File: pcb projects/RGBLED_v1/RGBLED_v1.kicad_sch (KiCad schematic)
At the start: 20 parts, among them J1 USB_B_Micro, J2 Conn_01x02_Pin, SW1 SW_Reed_SPDT, SW2 RESET BUTTON, U1 STM32F091RBTx, U2 LP3985IM5-3.3/NOPB

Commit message: changed switch, added swd jpg
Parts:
- removed SW1: SW_Reed_SPDT, symbol Switch:SW_Reed_SPDT
- added SW1: SW_DP3T, symbol Switch:SW_DP3T
- SW2: symbol Switch:SW_Push_Open_Dual -> Switch:SW_Push_Dual
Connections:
- net +3.3V: now also SW1.3
- net GND: now also SW2.1; no longer SW2.4
- net at C2.1, U2.5 (OUT): now also SW1.1
- net at BT1.1 (+): now also SW1.2
- no-connect marks 3 -> 4
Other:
- moved on the sheet: BT1

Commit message: board drawing, footprints except slide switch
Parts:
- added C9: 22nF, Capacitor_SMD:C_0805_2012Metric_Pad1.18x1.45mm_HandSolder, symbol Device:C
- BT1: footprint (none) -> Battery:BatteryHolder_MYOUNG_BS-07-A1BJ001_CR2032
- CN2: renamed from J2; value Conn_01x02_Pin -> Conn_01x03_Pin; footprint (none) -> Connector_PinHeader_2.54mm:PinHeader_1x03_P2.54mm_Vertical; symbol Connector:Conn_01x02_Pin -> Connector_Generic:Conn_01x03
- SW2: footprint (none) -> Button_Switch_SMD:SW_Push_1P1T_NO_E-Switch_TL3301NxxxxxG
- renumbered J1 to CN1
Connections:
- net GND: now also CN2.3 (Pin_3), C9.2
- net TCK: now also CN2.1 (Pin_1); no longer CN2.2 (Pin_2)
- net TMS: now also CN2.2 (Pin_2); no longer CN2.1 (Pin_1)
- net at BT1.1 (+), SW1.2: now also C9.1
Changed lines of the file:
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@@
+	)
+	(junction
+		(at 77.47 64.77)
+		(diameter 0)
+		(color 0 0 0 0)
 	)
 	(junction
@@
 	)
 	(junction
+		(at 77.47 76.2)
+		(diameter 0)
+		(color 0 0 0 0)
+	)
+	(junction
 		(at 220.98 151.13)
 		(diameter 0)
@@
 	(wire
 		(pts
+			(xy 77.47 64.77) (xy 77.47 68.58)
+		)
+		(stroke
+			(width 0)
+			(type default)
+		)
+	)
+	(wire
+		(pts
 			(xy 55.88 33.02) (xy 58.42 33.02)
 		)
@@
 	(wire
 		(pts
+			(xy 36.83 138.43) (xy 31.75 138.43)
+		)
+		(stroke
+			(width 0)
+			(type default)
+		)
+	)
+	(wire
+		(pts
 			(xy 229.87 33.02) (xy 243.84 33.02)
 		)
@@
 	(wire
 		(pts
+			(xy 31.75 138.43) (xy 31.75 139.7)
+		)
+		(stroke
+			(width 0)
+			(type default)
+		)
+	)
+	(wire
+		(pts
 			(xy 220.98 151.13) (xy 223.52 151.13)
 		)
@@
 	(wire
 		(pts
+			(xy 77.47 76.2) (xy 85.09 76.2)
+		)
+		(stroke
+			(width 0)
+			(type default)
+		)
+	)
+	(wire
+		(pts
 			(xy 215.9 54.61) (xy 215.9 50.8)
 		)
@@
 	(wire
 		(pts
-			(xy 77.47 57.15) (xy 77.47 68.58)
+			(xy 77.47 57.15) (xy 77.47 64.77)
 		)
 		(stroke
@@
 		(pts
 			(xy 24.13 54.61) (xy 31.75 54.61)
+		)
+		(stroke
+			(width 0)
+			(type default)
+		)
+	)
+	(wire
+		(pts
+			(xy 85.09 64.77) (xy 77.47 64.77)
+		)
+		(stroke
+			(width 0)
+			(type default)
+		)
+	)
+	(wire
+		(pts
+			(xy 85.09 68.58) (xy 85.09 64.77)
 		)
 		(stroke
@@
 			)
 		)
-		(property "Footprint" ""
+		(property "Footprint" "Button_Switch_SMD:SW_Push_1P1T_NO_E-Switch_TL3301NxxxxxG"
 			(at 39.37 100.33 0)
 			(effects
@@
 	)
 	(symbol
+		(lib_id "Device:C")
+		(at 85.09 72.39 0)
+		(unit 1)
+		(exclude_from_sim no)
+		(in_bom yes)
+		(on_board yes)
+		(dnp no)
+		(fields_autoplaced yes)
+		(property "Reference" "C9"
+			(at 88.9 71.1199 0)
+			(effects
+				(font
+					(size 1.27 1.27)
+				)
+				(justify left)
+			)
+		)
+		(property "Value" "22nF"
+			(at 88.9 73.6599 0)
+			(effects
+				(font
+					(size 1.27 1.27)
+				)
+				(justify left)
+			)
+		)
+		(property "Footprint" "Capacitor_SMD:C_0805_2012Metric_Pad1.18x1.45mm_HandSolder"
+			(at 86.0552 76.2 0)
+			(effects
+				(font
+					(size 1.27 1.27)
+				)
+				(hide yes)
+			)
+		)
+		(property "Datasheet" "~"
+			(at 85.09 72.39 0)
+			(effects
+				(font
+					(size 1.27 1.27)
+				)
+				(hide yes)
+			)
+		)
+		(property "Description" "Unpolarized capacitor"
+			(at 85.09 72.39 0)
+			(effects
+				(font
+					(size 1.27 1.27)
+				)
+				(hide yes)
+			)
+		)
+		(pin "2"
+		)
+		(pin "1"
+		)
+		(instances
+			(project ""
+				(path "/776e18e0-dd51-4c38-87d7-7b7a4ed2b66e"
+					(reference "C9")
+					(unit 1)
+				)
+			)
+		)
+	)
+	(symbol
 		(lib_id "power:+3.3V")
 		(at 229.87 21.59 0)
@@
 	)
 	(symbol
-		(lib_id "power:+3.3V")
-		(at 198.12 54.61 0)
-		(unit 1)
-		(exclude_from_sim no)
-		(in_bom yes)
-		(on_board yes)
-		(dnp no)
-		(fields_autoplaced yes)
-		(property "Reference" "#PWR012"
-			(at 198.12 58.42 0)
-			(effects
-				(font
-					(size 1.27 1.27)
-				)
-				(hide yes)
-			)
-		)
-		(property "Value" "+3.3V"
-			(at 198.12 49.53 0)
-			(effects
-				(font
-					(size 1.27 1.27)
-				)
-			)
-		)
-		(property "Footprint" ""
-			(at 198.12 54.61 0)
-			(effects
-				(font
-					(size 1.27 1.27)
-				)
-				(hide yes)
-			)
-		)
-		(property "Datasheet" ""
-			(at 198.12 54.61 0)
-			(effects
-				(font
-					(size 1.27 1.27)
-				)
-				(hide yes)
-			)
-		)
-		(property "Description" "Power symbol creates a global label with name \"+3.3V\""
-			(at 198.12 54.61 0)
-			(effects
-				(font
-					(size 1.27 1.27)
-				)
-				(hide yes)
-			)
-		)
-		(pin "1"
-		)
-		(instances
-			(project "RGBLED_v1"
-				(path "/776e18e0-dd51-4c38-87d7-7b7a4ed2b66e"
-					(reference "#PWR012")
-					(unit 1)
-				)
-			)
-		)
-	)
-	(symbol
 		(lib_id "Device:Battery_Cell")
 		(at 77.47 73.66 0)
@@
 			)
 		)
-		(property "Footprint" ""
+		(property "Footprint" "Battery:BatteryHolder_MYOUNG_BS-07-A1BJ001_CR2032"
 			(at 77.47 72.136 90)
 			(effects
@@
 		(dnp no)
 		(fields_autoplaced yes)
-		(property "Reference" "J1"
-			(at 36.83 29.2099 90)
+		(property "Reference" "CN1"
+			(at 36.83 30.4799 90)
 			(effects
 				(font
@@
 				)
 				(justify left)
+				(hide yes)
 			)
 		)
@@
 			(project ""
 				(path "/776e18e0-dd51-4c38-87d7-7b7a4ed2b66e"
-					(reference "J1")
+					(reference "CN1")
 					(unit 1)
 				)
@@
 	)
 	(symbol
-		(lib_id "Connector:Conn_01x02_Pin")
-		(at 41.91 135.89 180)
+		(lib_id "Connector_Generic:Conn_01x03")
+		(at 41.91 135.89 0)
 		(unit 1)
 		(exclude_from_sim no)
@@
 		(dnp no)
 		(fields_autoplaced yes)
-		(property "Reference" "J2"
-			(at 43.18 133.3499 0)
-			(effects
-				(font
-					(size 1.27 1.27)
-				)
-				(justify right)
-			)
-		)
-		(property "Value" "Conn_01x02_Pin"
-			(at 43.18 135.8899 0)
-			(effects
-				(font
-					(size 1.27 1.27)
-				)
-				(justify right)
-			)
-		)
-		(property "Footprint" ""
+		(property "Reference" "CN2"
+			(at 44.45 135.8899 0)
+			(effects
+				(font
+					(size 1.27 1.27)
+				)
+				(justify left)
+			)
+		)
+		(property "Value" "Conn_01x03_Pin"
+			(at 44.45 137.1599 0)
+			(effects
+				(font
+					(size 1.27 1.27)
+				)
+				(justify left)
+				(hide yes)
+			)
+		)
+		(property "Footprint" "Connector_PinHeader_2.54mm:PinHeader_1x03_P2.54mm_Vertical"
 			(at 41.91 135.89 0)
 			(effects
@@
 			)
 		)
-		(property "Description" "Generic connector, single row, 01x02, script generated"
+		(property "Description" "Generic connector, single row, 01x03, script generated (kicad-library-utils/schlib/autogen/connector/)"
 			(at 41.91 135.89 0)
 			(effects
@@
 		)
 		(pin "2"
+		)
+		(pin "3"
 		)
 		(instances
 			(project ""
 				(path "/776e18e0-dd51-4c38-87d7-7b7a4ed2b66e"
-					(reference "J2")
+					(reference "CN2")
 					(unit 1)
 				)
@@
 					(unit 1)
 				)
+			)
+		)
+	)
+	(symbol
+		(lib_id "power:GND")
+		(at 31.75 139.7 0)
+		(mirror y)
+		(unit 1)
+		(exclude_from_sim no)
+		(in_bom yes)
+		(on_board yes)
+		(dnp no)
+		(fields_autoplaced yes)
+		(property "Reference" "#PWR015"
+			(at 31.75 146.05 0)
+			(effects
+				(font
+					(size 1.27 1.27)
+				)
+				(hide yes)
+			)
+		)
+		(property "Value" "GND"
+			(at 31.75 144.78 0)
+			(effects
+				(font
+					(size 1.27 1.27)
+				)
+			)
+		)
+		(property "Footprint" ""
+			(at 31.75 139.7 0)
+			(effects
+				(font
+					(size 1.27 1.27)
+				)
+				(hide yes)
+			)
+		)
+		(property "Datasheet" ""
+			(at 31.75 139.7 0)
+			(effects
+				(font
+					(size 1.27 1.27)
+				)
+				(hide yes)
+			)
+		)
+		(property "Description" "Power symbol creates a global label with name \"GND\" , ground"
+			(at 31.75 139.7 0)
+			(effects
+				(font
+					(size 1.27 1.27)
+				)
+				(hide yes)
+			)
+		)
+		(pin "1"
+		)
+		(instances
+			(project "RGBLED_v1"
+				(path "/776e18e0-dd51-4c38-87d7-7b7a4ed2b66e"
+					(reference "#PWR015")
+					(unit 1)
+				)

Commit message: mcu finished
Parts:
- removed SW1: SW_DP3T, symbol Switch:SW_DP3T
- removed SW2: RESET BUTTON, Button_Switch_SMD:SW_Push_1P1T_NO_E-Switch_TL3301NxxxxxG, symbol Switch:SW_Push_Dual
- added C10, C11: 4.3pF, Capacitor_SMD:C_1206_3216Metric_Pad1.33x1.80mm_HandSolder, symbol Device:C
- added C12: 100nF, symbol Device:C
- added J1: Conn_02x02_Odd_Even, Connector_PinHeader_2.54mm:PinHeader_2x02_P2.54mm_Vertical, symbol Connector_Generic:Conn_02x02_Odd_Even
- added JP1: SolderJumper, Jumper:SolderJumper-2_P1.3mm_Open_TrianglePad1.0x1.5mm, symbol Jumper:SolderJumper_2_Open
- added L1: Ferrite, symbol Device:L
- added SW1: SW_MEC_5E, Button_Switch_SMD:SW_MEC_5GSH9, symbol Switch:SW_MEC_5E
- added Y1: 32.768kHz, Crystal:Crystal_SMD_HC49-SD_HandSoldering, symbol Device:Crystal
- C4, C5, C6, C7, C8: value 0.01uF -> 100nF
- C9: footprint Capacitor_SMD:C_0805_2012Metric_Pad1.18x1.45mm_HandSolder -> Capacitor_SMD:C_1206_3216Metric_Pad1.33x1.80mm_HandSolder
- CN2: footprint Connector_PinHeader_2.54mm:PinHeader_1x03_P2.54mm_Vertical -> Connector_PinHeader_2.54mm:PinHeader_1x04_P2.54mm_Vertical; symbol Connector_Generic:Conn_01x03 -> Connector_Generic:Conn_01x04
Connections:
- net +3.3V: now also CN2.1 (Pin_1), J1.2 (Pin_2), J1.4 (Pin_4), L1.1; no longer C7.2, U1.13 (VDDA), U1.48 (VDDIO2)
- net GND: now also CN2.4 (Pin_4), C10.1, C11.2, C12.1, JP1.1 (A), SW1.1, SW1.2; no longer C7.1, CN2.3 (Pin_3), U1.12 (VSSA)
- net TCK: now also CN2.2 (Pin_2); no longer CN2.1 (Pin_1)
- net TMS: now also CN2.3 (Pin_3); no longer CN2.2 (Pin_2)
- net nRST: now also C12.2, SW1.3 (K), SW1.4 (A)
- net at U1.3 (PC14): now also C10.2, Y1.2
- net at U1.4 (PC15): now also C11.1, Y1.1
- net at C2.1, U2.5 (OUT): now also J1.1 (Pin_1)
- net at BT1.1 (+), C9.1: now also J1.3 (Pin_3)
- new net AVDD: C7.2, L1.2, U1.13 (VDDA)
- new net GNDA: C7.1, JP1.2 (B), U1.12 (VSSA)
- no-connect marks 4 -> 3
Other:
- moved on the sheet: C7

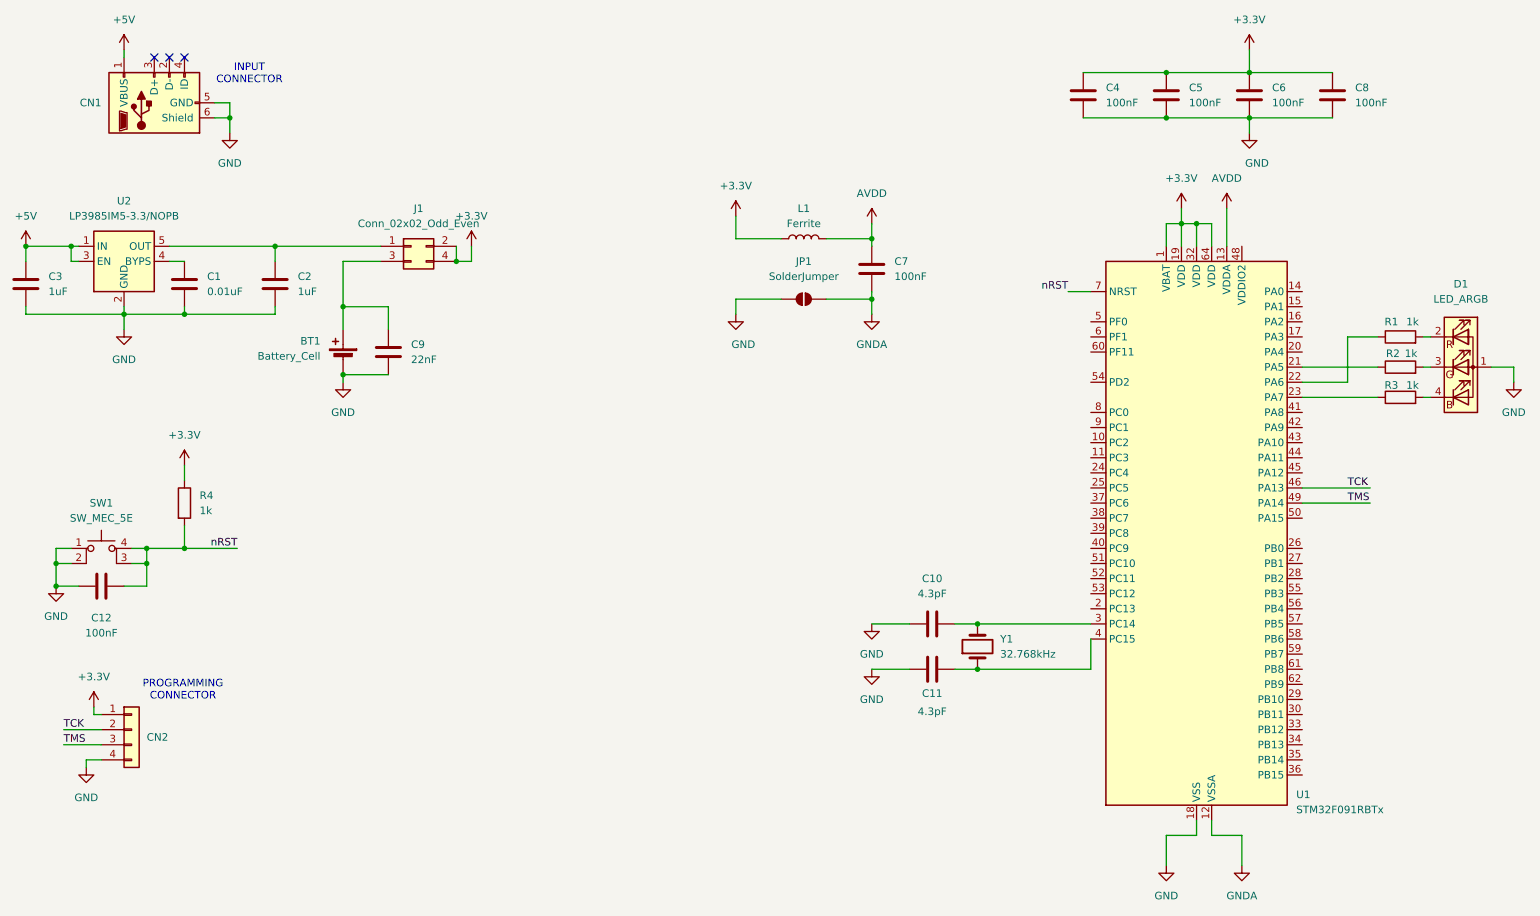
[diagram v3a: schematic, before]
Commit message: components placement
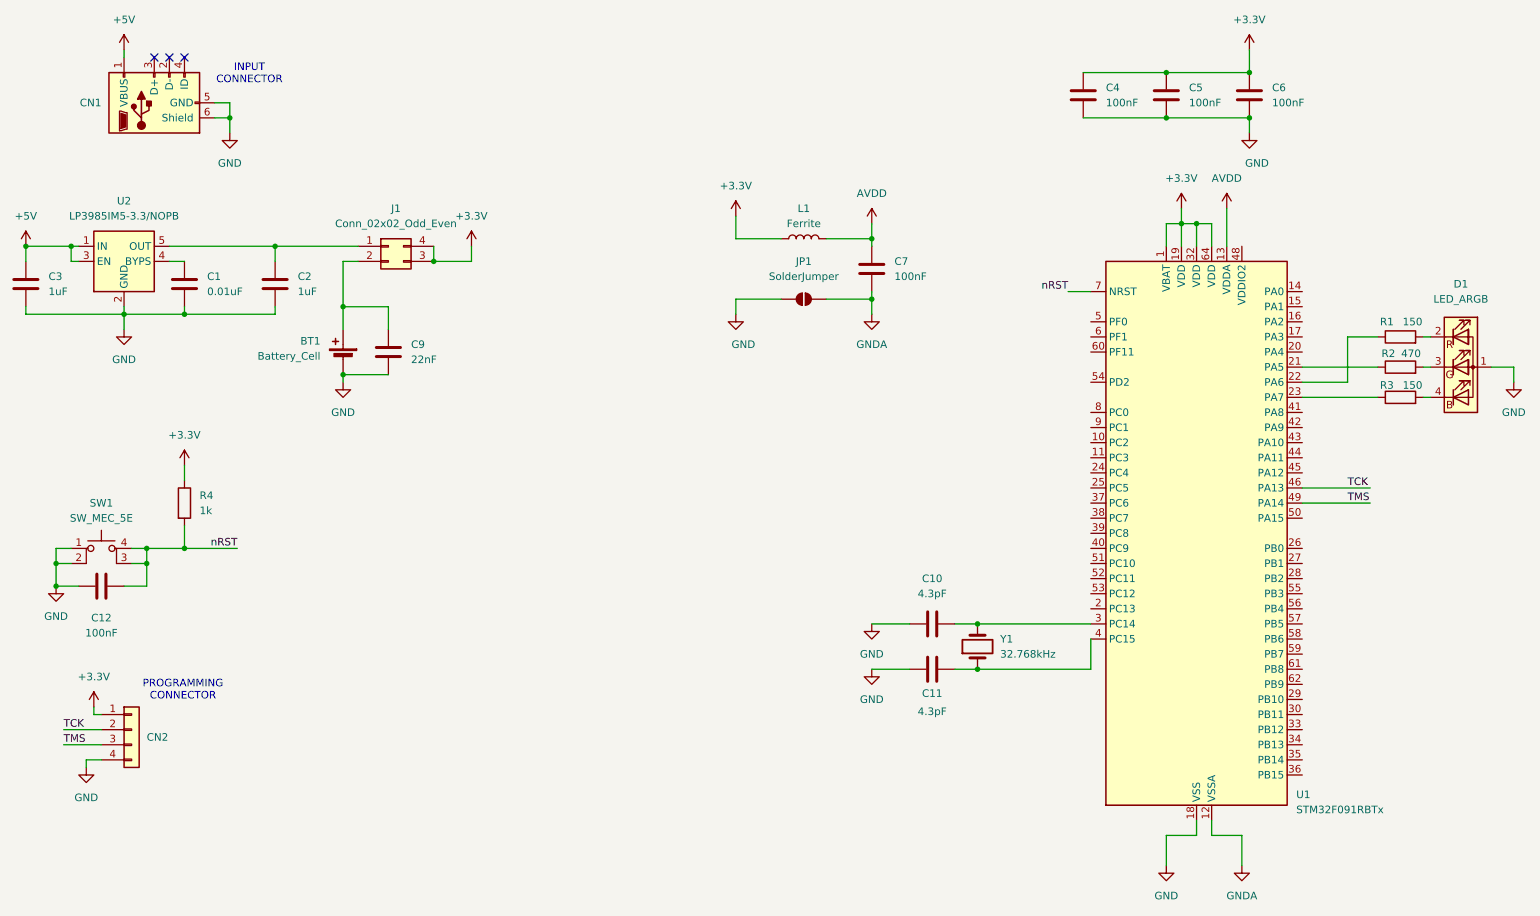
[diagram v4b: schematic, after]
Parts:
- removed C8: 100nF, Capacitor_SMD:C_1206_3216Metric_Pad1.33x1.80mm_HandSolder, symbol Device:C
- J1: symbol Connector_Generic:Conn_02x02_Odd_Even -> Connector_Generic:Conn_02x02_Counter_Clockwise
- R1, R3: value 1k -> 150
- R2: value 1k -> 470
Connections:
- net +3.3V: now also J1.3 (Pin_3); no longer J1.2 (Pin_2)
- net at BT1.1 (+), C9.1: now also J1.2 (Pin_2); no longer J1.3 (Pin_3)
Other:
- moved on the sheet: J1
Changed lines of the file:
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@@
 	)
 	(junction
-		(at 66.04 54.61)
+		(at 220.98 50.8)
 		(diameter 0)
 		(color 0 0 0 0)
 	)
 	(junction
-		(at 220.98 50.8)
+		(at 184.15 125.73)
 		(diameter 0)
 		(color 0 0 0 0)
 	)
 	(junction
-		(at 184.15 125.73)
+		(at 66.04 54.61)
 		(diameter 0)
 		(color 0 0 0 0)
@@
 	)
 	(junction
-		(at 96.52 57.15)
-		(diameter 0)
-		(color 0 0 0 0)
-	)
-	(junction
 		(at 40.64 66.04)
 		(diameter 0)
@@
 	)
 	(junction
+		(at 92.71 57.15)
+		(diameter 0)
+		(color 0 0 0 0)
+	)
+	(junction
 		(at 229.87 33.02)
 		(diameter 0)
@@
 	(wire
 		(pts
-			(xy 223.52 50.8) (xy 223.52 54.61)
+			(xy 92.71 54.61) (xy 92.71 57.15)
 		)
 		(stroke
@@
 	(wire
 		(pts
-			(xy 24.13 64.77) (xy 24.13 66.04)
+			(xy 223.52 50.8) (xy 223.52 54.61)
 		)
 		(stroke
@@
 	(wire
 		(pts
-			(xy 66.04 66.04) (xy 50.8 66.04)
+			(xy 24.13 64.77) (xy 24.13 66.04)
 		)
 		(stroke
@@
 	(wire
 		(pts
-			(xy 203.2 120.65) (xy 203.2 125.73)
+			(xy 66.04 66.04) (xy 50.8 66.04)
 		)
 		(stroke
@@
 	(wire
 		(pts
-			(xy 34.29 140.97) (xy 36.83 140.97)
+			(xy 203.2 120.65) (xy 203.2 125.73)
 		)
 		(stroke
@@
 	(wire
 		(pts
-			(xy 29.21 107.95) (xy 29.21 111.76)
+			(xy 34.29 140.97) (xy 36.83 140.97)
 		)
 		(stroke
@@
 	(wire
 		(pts
-			(xy 238.76 80.01) (xy 251.46 80.01)
+			(xy 29.21 107.95) (xy 29.21 111.76)
 		)
 		(stroke
@@
 	(wire
 		(pts
-			(xy 228.6 153.67) (xy 223.52 153.67)
+			(xy 238.76 80.01) (xy 251.46 80.01)
 		)
 		(stroke
@@
 	(wire
 		(pts
-			(xy 229.87 33.02) (xy 243.84 33.02)
+			(xy 228.6 153.67) (xy 223.52 153.67)
 		)
 		(stroke
@@
 	(wire
 		(pts
-			(xy 77.47 57.15) (xy 83.82 57.15)
+			(xy 77.47 57.15) (xy 80.01 57.15)
 		)
 		(stroke
@@
 	(wire
 		(pts
-			(xy 66.04 54.61) (xy 83.82 54.61)
-		)
-		(stroke
-			(width 0)
-			(type default)
-		)
-	)
-	(wire
-		(pts
 			(xy 29.21 105.41) (xy 29.21 107.95)
 		)
@@
 	(wire
 		(pts
-			(xy 229.87 25.4) (xy 243.84 25.4)
-		)
-		(stroke
-			(width 0)
-			(type default)
-		)
-	)
-	(wire
-		(pts
 			(xy 77.47 76.2) (xy 85.09 76.2)
 		)
@@
 	(wire
 		(pts
-			(xy 96.52 57.15) (xy 99.06 57.15)
+			(xy 24.13 54.61) (xy 31.75 54.61)
 		)
 		(stroke
@@
 	(wire
 		(pts
-			(xy 24.13 54.61) (xy 31.75 54.61)
+			(xy 85.09 64.77) (xy 77.47 64.77)
 		)
 		(stroke
@@
 	(wire
 		(pts
-			(xy 85.09 64.77) (xy 77.47 64.77)
+			(xy 143.51 63.5) (xy 143.51 66.04)
 		)
 		(stroke
@@
 	(wire
 		(pts
-			(xy 143.51 63.5) (xy 143.51 66.04)
+			(xy 85.09 68.58) (xy 85.09 64.77)
 		)
 		(stroke
@@
 	(wire
 		(pts
-			(xy 96.52 54.61) (xy 96.52 57.15)
+			(xy 66.04 54.61) (xy 80.01 54.61)
 		)
 		(stroke
@@
 	(wire
 		(pts
-			(xy 85.09 68.58) (xy 85.09 64.77)
+			(xy 31.75 54.61) (xy 33.02 54.61)
 		)
 		(stroke
@@
 	(wire
 		(pts
-			(xy 31.75 54.61) (xy 33.02 54.61)
+			(xy 92.71 57.15) (xy 99.06 57.15)
 		)
 		(stroke
@@
 		(dnp no)
 		(property "Reference" "R2"
-			(at 254 72.644 90)
+			(at 253.238 72.644 90)
 			(effects
 				(font
@@
 			)
 		)
-		(property "Value" "1k"
+		(property "Value" "470"
 			(at 257.048 72.644 90)
 			(effects
@@
 	)
 	(symbol
-		(lib_id "Device:C")
-		(at 243.84 29.21 180)
-		(unit 1)
-		(exclude_from_sim no)
-		(in_bom yes)
-		(on_board yes)
-		(dnp no)
-		(fields_autoplaced yes)
-		(property "Reference" "C8"
-			(at 247.65 27.9399 0)
-			(effects
-				(font
-					(size 1.27 1.27)
-				)
-				(justify right)
-			)
-		)
-		(property "Value" "100nF"
-			(at 247.65 30.4799 0)
-			(effects
-				(font
-					(size 1.27 1.27)
-				)
-				(justify right)
-			)
-		)
-		(property "Footprint" "Capacitor_SMD:C_1206_3216Metric_Pad1.33x1.80mm_HandSolder"
-			(at 242.8748 25.4 0)
-			(effects
-				(font
-					(size 1.27 1.27)
-				)
-				(hide yes)
-			)
-		)
-		(property "Datasheet" "~"
-			(at 243.84 29.21 0)
-			(effects
-				(font
-					(size 1.27 1.27)
-				)
-				(hide yes)
-			)
-		)
-		(property "Description" "Unpolarized capacitor"
-			(at 243.84 29.21 0)
-			(effects
-				(font
-					(size 1.27 1.27)
-				)
-				(hide yes)
-			)
-		)
-		(pin "2"
-		)
-		(pin "1"
-		)
-		(instances
-			(project "RGBLED_v1"
-				(path "/776e18e0-dd51-4c38-87d7-7b7a4ed2b66e"
-					(reference "C8")
-					(unit 1)
-				)
-			)
-		)
-	)
-	(symbol
 		(lib_id "power:GND")
 		(at 29.21 111.76 0)
@@
 		(dnp no)
 		(property "Reference" "R3"
-			(at 253.746 77.978 90)
+			(at 252.984 77.978 90)
 			(effects
 				(font
@@
 			)
 		)
-		(property "Value" "1k"
+		(property "Value" "150"
 			(at 257.302 77.978 90)
 			(effects
@@
 	)
 	(symbol
-		(lib_id "Connector_Generic:Conn_02x02_Odd_Even")
-		(at 88.9 54.61 0)
+		(lib_id "Connector_Generic:Conn_02x02_Counter_Clockwise")
+		(at 85.09 54.61 0)
 		(unit 1)
 		(exclude_from_sim no)
@@
 		(fields_autoplaced yes)
 		(property "Reference" "J1"
-			(at 90.17 48.26 0)
+			(at 86.36 48.26 0)
 			(effects
 				(font
@@
 		)
 		(property "Value" "Conn_02x02_Odd_Even"
-			(at 90.17 50.8 0)
+			(at 86.36 50.8 0)
 			(effects
 				(font
@@
 		)
 		(property "Footprint" "Connector_PinHeader_2.54mm:PinHeader_2x02_P2.54mm_Vertical"
-			(at 88.9 54.61 0)
+			(at 85.09 54.61 0)
 			(effects
 				(font
@@
 		)
 		(property "Datasheet" "~"
-			(at 88.9 54.61 0)
+			(at 85.09 54.61 0)
 			(effects
 				(font
@@
 			)
 		)
-		(property "Description" "Generic connector, double row, 02x02, odd/even pin numbering scheme (row 1 odd numbers, row 2 even numbers), script generated (kicad-library-utils/schlib/autogen/connector/)"
-			(at 88.9 54.61 0)
+		(property "Description" "Generic connector, double row, 02x02, counter clockwise pin numbering scheme (similar to DIP package numbering), script generated (kicad-library-utils/schlib/autogen/connector/)"
+			(at 85.09 54.61 0)
 			(effects
 				(font
@@
 		(dnp no)
 		(property "Reference" "R1"
-			(at 253.746 67.31 90)
+			(at 252.984 67.31 90)
 			(effects
 				(font
@@
 			)
 		)
-		(property "Value" "1k"
+		(property "Value" "150"
 			(at 257.302 67.31 90)
 			(effects
